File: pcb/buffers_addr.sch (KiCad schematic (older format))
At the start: 8 parts

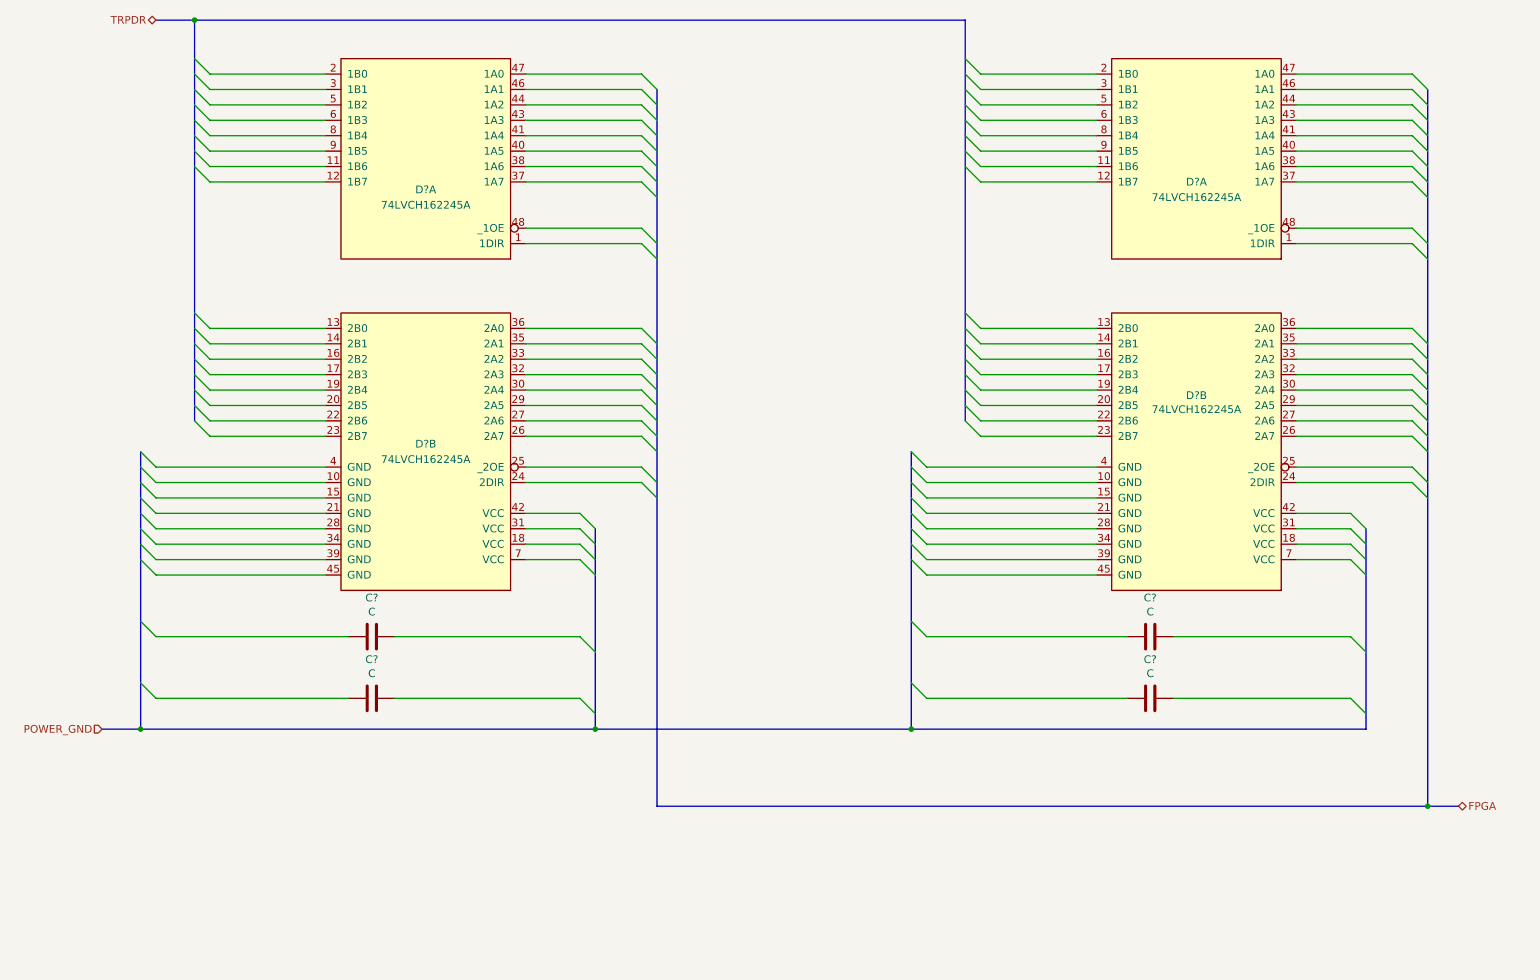
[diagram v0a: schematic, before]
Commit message: buffer section finished, audio moved to expansion connector
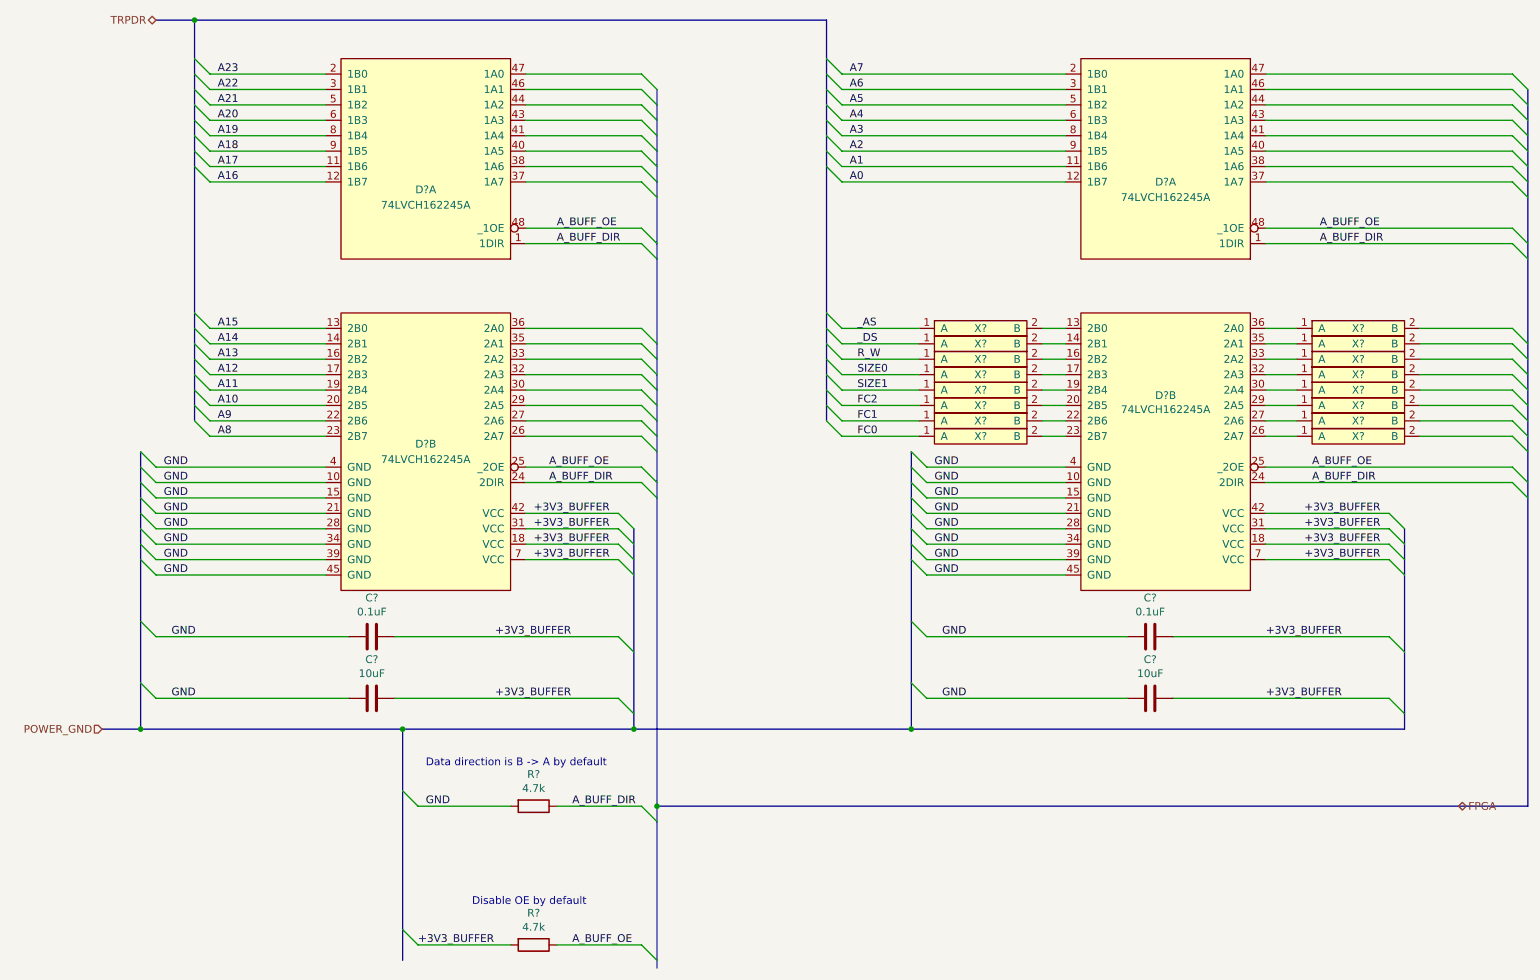
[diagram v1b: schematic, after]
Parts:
- added R? (x2): 4.7k, symbol Device:R
- added X? (x16): testpoint_cutline, symbol WM1200:testpoint_cutline
- C? (x2): value C -> 10uF
- C? (x2): value C -> 0.1uF
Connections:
- net A_BUFF_DIR: now reaches D?.1 (1DIR)
- net A_BUFF_DIR: now also D?.1 (1DIR), D?.24 (2DIR), D?.24 (2DIR), R?.1
- net A17: now reaches D?.11 (1B6)
- net A16: now reaches D?.12 (1B7)
- net A23: now reaches D?.2 (1B0)
- net A22: now reaches D?.3 (1B1)
- net A_BUFF_OE: now reaches D?.48 (_1OE)
- net A_BUFF_OE: now also D?.25 (_2OE), D?.25 (_2OE), D?.48 (_1OE), R?.1
- net A21: now reaches D?.5 (1B2)
- net A20: now reaches D?.6 (1B3)
- net A19: now reaches D?.8 (1B4)
- net A18: now reaches D?.9 (1B5)
- net GND: now reaches D?.10 (GND)
- net GND: now also C?.1, C?.1, C?.1, C?.1, D?.10 (GND), D?.15 (GND), D?.15 (GND), D?.21 (GND), D?.21 (GND), D?.28 (GND), D?.28 (GND), D?.34 (GND), D?.34 (GND), D?.39 (GND), D?.39 (GND), D?.4 (GND), D?.4 (GND), D?.45 (GND), D?.45 (GND), R?.2
- net A15: now reaches D?.13 (2B0)
- net A14: now reaches D?.14 (2B1)
- net A13: now reaches D?.16 (2B2)
- net A12: now reaches D?.17 (2B3)
- net +3V3_BUFFER: now reaches D?.18 (VCC)
- net +3V3_BUFFER: now also C?.2, C?.2, C?.2, C?.2, D?.18 (VCC), D?.31 (VCC), D?.31 (VCC), D?.42 (VCC), D?.42 (VCC), D?.7 (VCC), D?.7 (VCC), R?.2
- net A11: now reaches D?.19 (2B4)
- net A10: now reaches D?.20 (2B5)
- net A9: now reaches D?.22 (2B6)
- net A8: now reaches D?.23 (2B7)
- net A1: now reaches D?.11 (1B6)
- net A0: now reaches D?.12 (1B7)
- net A7: now reaches D?.2 (1B0)
- net A6: now reaches D?.3 (1B1)
- net A5: now reaches D?.5 (1B2)
- net A4: now reaches D?.6 (1B3)
- net A3: now reaches D?.8 (1B4)
- net A2: now reaches D?.9 (1B5)
- net at D?.13 (2B0): now also X?.2 (B)
- net at D?.14 (2B1): now also X?.2 (B)
- net at D?.16 (2B2): now also X?.2 (B)
- net at D?.17 (2B3): now also X?.2 (B)
- net at D?.19 (2B4): now also X?.2 (B)
- net at D?.20 (2B5): now also X?.2 (B)
- net at D?.22 (2B6): now also X?.2 (B)
- net at D?.23 (2B7): now also X?.2 (B)
- net at D?.26 (2A7): now also X?.1 (A)
- net at D?.27 (2A6): now also X?.1 (A)
- net at D?.29 (2A5): now also X?.1 (A)
- net at D?.30 (2A4): now also X?.1 (A)
- net at D?.32 (2A3): now also X?.1 (A)
- net at D?.33 (2A2): now also X?.1 (A)
- net at D?.35 (2A1): now also X?.1 (A)
- net at D?.36 (2A0): now also X?.1 (A)
- new net FC0: X?.1 (A)
- new net FC1: X?.1 (A)
- new net FC2: X?.1 (A)
- new net R_W: X?.1 (A)
- new net SIZE0: X?.1 (A)
- new net SIZE1: X?.1 (A)
- new net _AS: X?.1 (A)
- new net _DS: X?.1 (A)
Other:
- note added: "Data direction is B -> A by default"
- note added: "Disable OE by default"
- moved on the sheet: D?A, D?B
